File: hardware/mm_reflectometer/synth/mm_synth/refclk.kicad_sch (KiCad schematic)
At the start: 25 parts

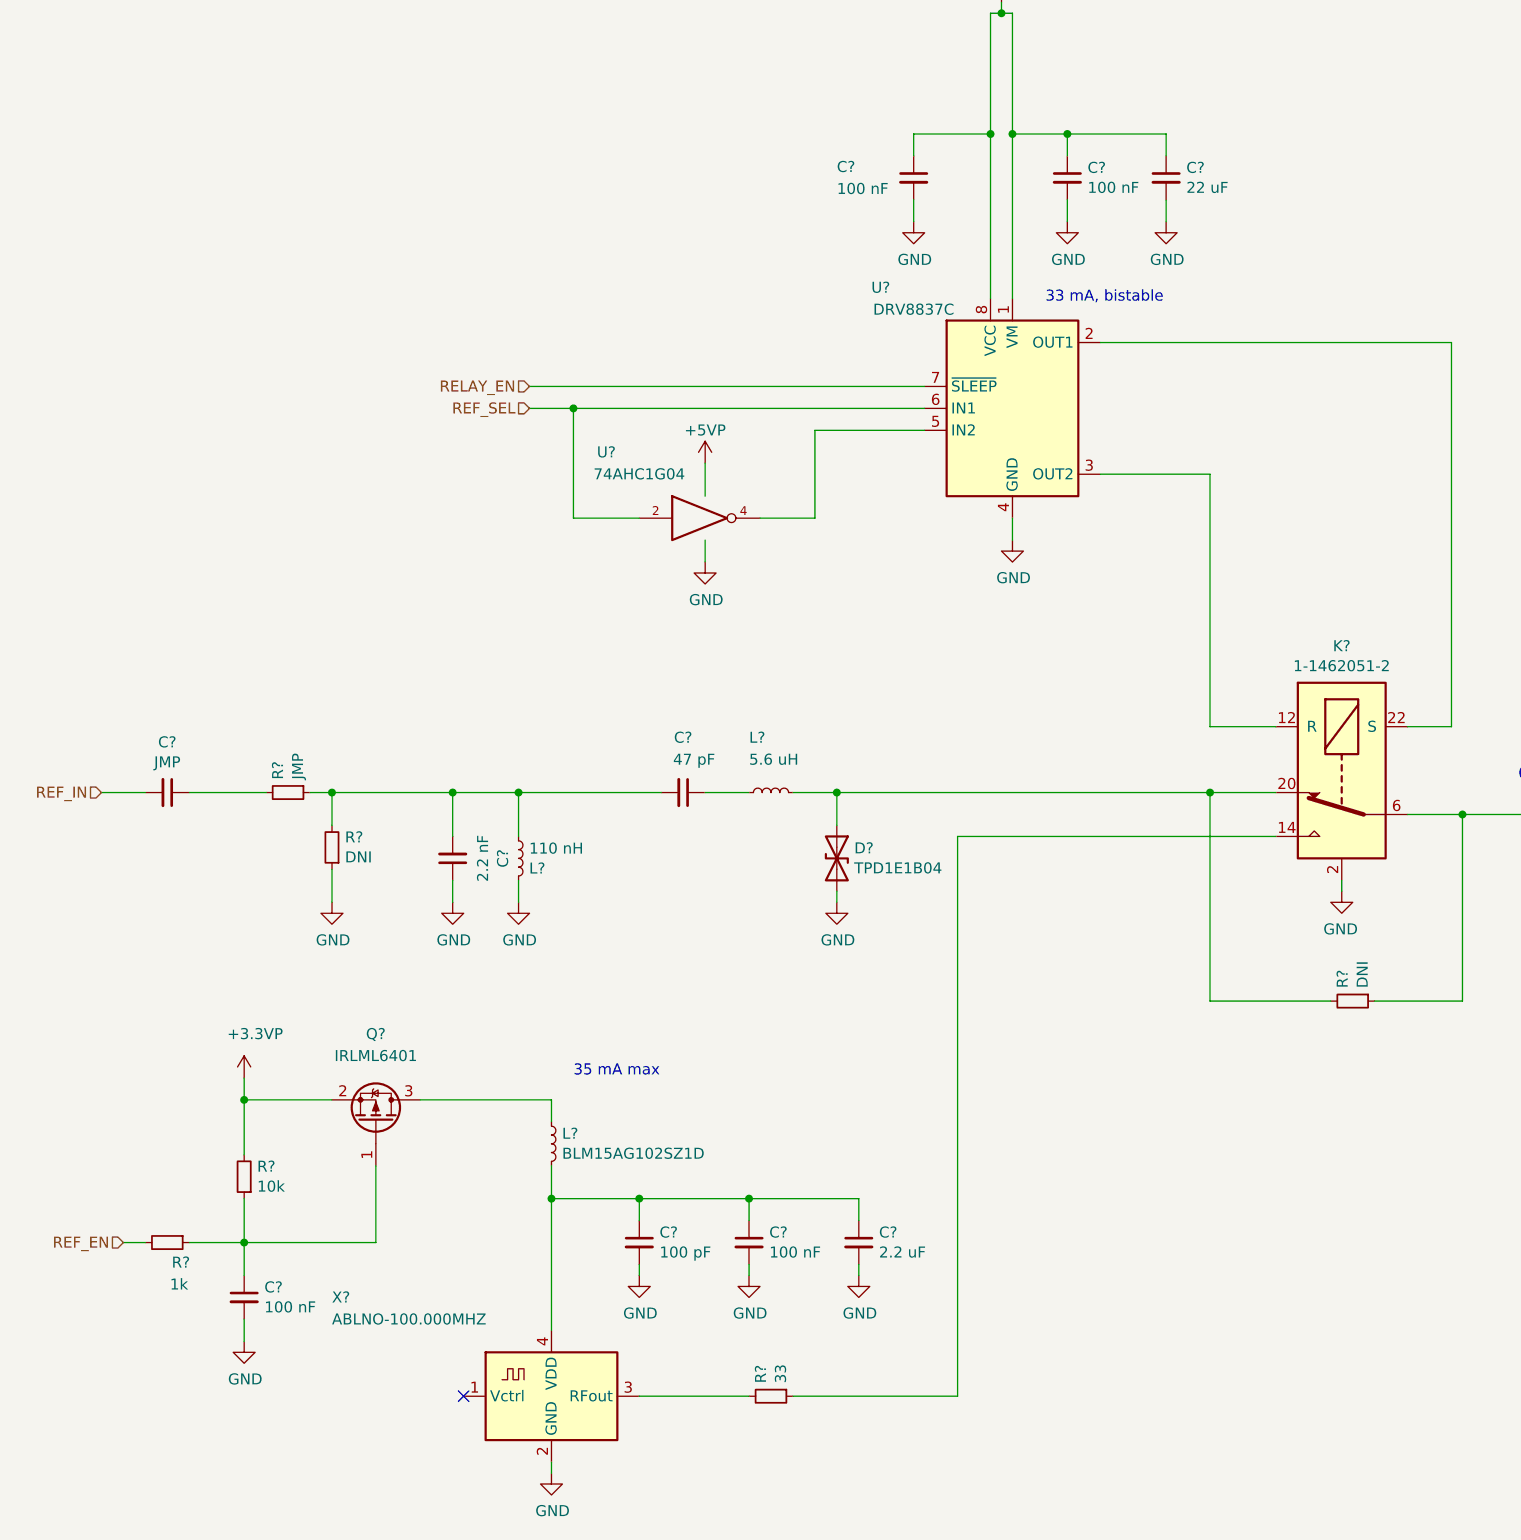
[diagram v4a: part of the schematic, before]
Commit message: work on mm synth schematic - control signals and footprint assignments
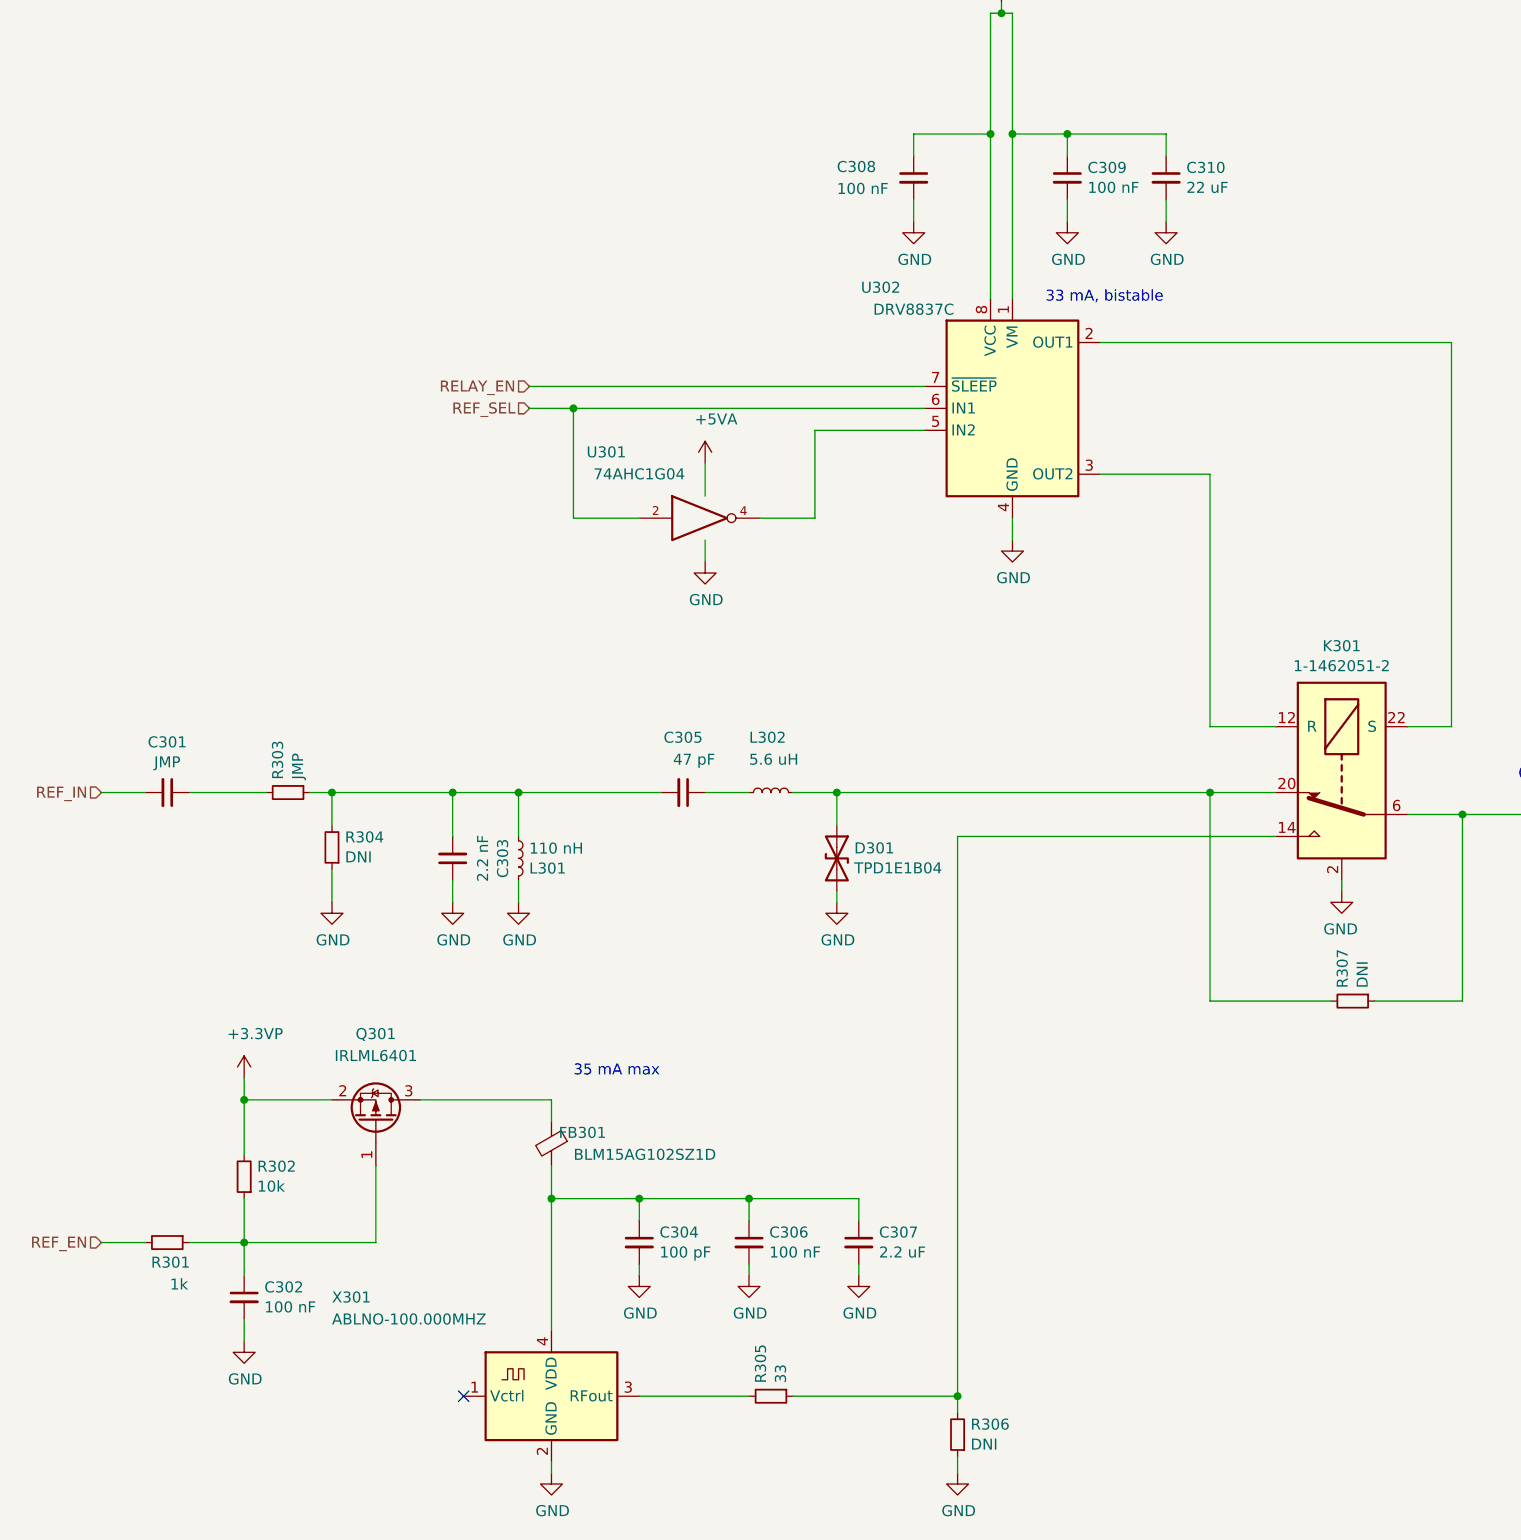
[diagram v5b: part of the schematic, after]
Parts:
- removed L?: BLM15AG102SZ1D, Inductor_SMD:L_0402_1005Metric, symbol Device:L_Small
- added FB301: BLM15AG102SZ1D, symbol Device:FerriteBead_Small
- added R306: DNI, Resistor_SMD:R_0402_1005Metric, symbol Device:R_Small
- gave numbers to parts that had none: 24
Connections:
- net +5VP is gone; now on net +5VA: U301.5 (VCC)
- net GND: now also R306.1
- net at Q301.3 (D): now also FB301.1
- net at C304.1, C306.1, C307.1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: now also FB301.2
- net at K301.14, R305.1: now also R306.2

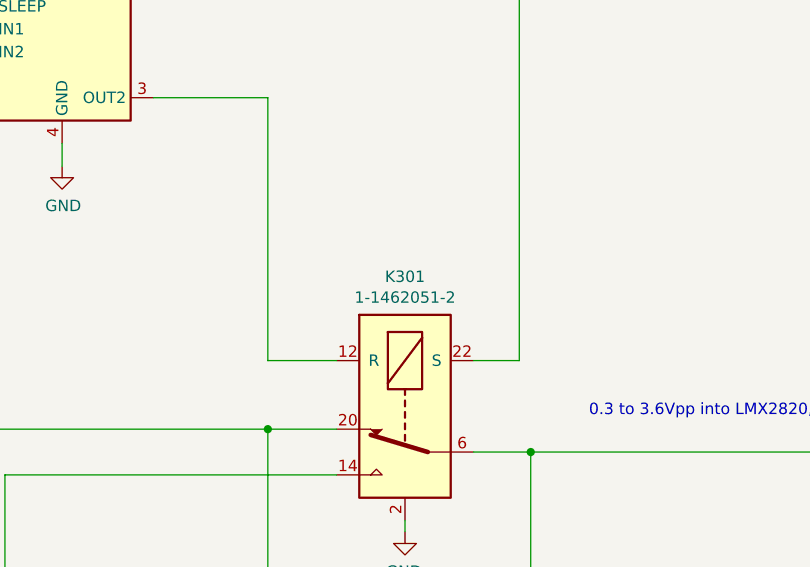
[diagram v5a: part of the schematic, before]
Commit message: added aux high speed io connector, fixed hierarchical buses
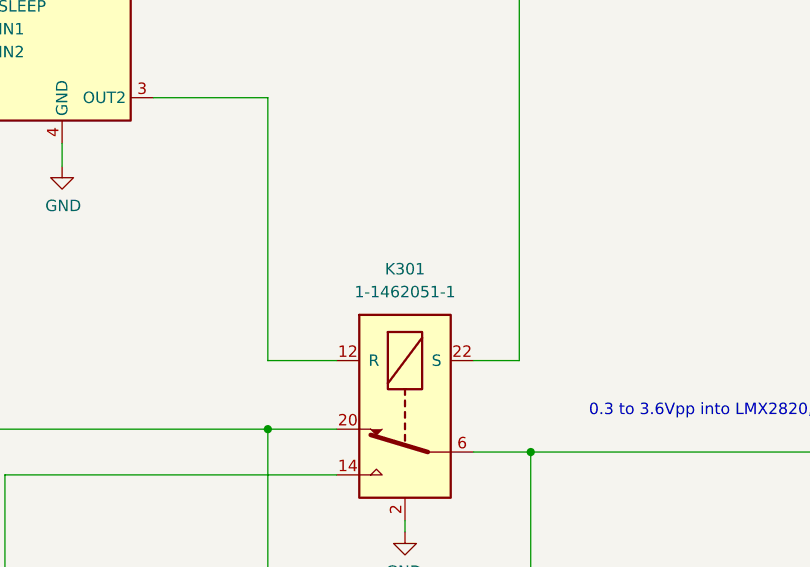
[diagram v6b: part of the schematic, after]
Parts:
- removed K301: 1-1462051-2, Relay_SMD:Relay_SPDT_AXICOM_HF3Series_50ohms_Pitch1.27mm, symbol vna_mm_ref-rescue:1-1462051-1-vna_mm
- added K301: 1-1462051-1, Relay_SMD:Relay_SPDT_AXICOM_HF3Series_50ohms_Pitch1.27mm, symbol vna_mm:1-1462051-1
- FB301: footprint (none) -> Inductor_SMD:L_0402_1005Metric
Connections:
- net GND: now also K301.10, K301.13, K301.15, K301.17, K301.19, K301.2, K301.21, K301.5, K301.7
- net OSC_OUT: now also K301.6
- net at U302.2 (OUT1): now also K301.11, K301.22 (S)
- net at U302.3 (OUT2): now also K301.1, K301.12 (R)
- net at R305.1, R306.2: now also K301.14
- net at D301.1 (A1), L302.1, R307.2: now also K301.20
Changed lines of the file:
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@@
       (effects (font (size 1.27 1.27)) (justify left))
     )
-    (property "Footprint" "" (id 2) (at 83.058 151.13 90)
+    (property "Footprint" "Inductor_SMD:L_0402_1005Metric" (id 2) (at 83.058 151.13 90)
       (effects (font (size 1.27 1.27)) hide)
     )
@@
     (pin "4")
   )
-  (symbol (lib_id "vna_mm_ref-rescue:1-1462051-1-vna_mm") (at 171.45 107.95 0) (mirror y) (unit 1)
-    (in_bom yes) (on_board yes)
-    (property "Reference" "K301" (id 0) (at 172.72 93.5482 0))
-    (property "Value" "1-1462051-2" (id 1) (at 172.72 95.8596 0))
+  (symbol (lib_id "vna_mm:1-1462051-1") (at 171.45 107.95 0) (mirror y) (unit 1)
+    (in_bom yes) (on_board yes) (fields_autoplaced)
+    (property "Reference" "K301" (id 0) (at 172.72 92.71 0))
+    (property "Value" "1-1462051-1" (id 1) (at 172.72 95.25 0))
     (property "Footprint" "Relay_SMD:Relay_SPDT_AXICOM_HF3Series_50ohms_Pitch1.27mm" (id 2) (at 182.88 93.98 0)
       (effects (font (size 1.27 1.27)) (justify left) hide)
@@
       (effects (font (size 1.27 1.27)) hide)
     )
-    (property "DIST_NAME" "Digi-Key" (id 4) (at 171.45 107.95 0)
-      (effects (font (size 1.27 1.27)) hide)
-    )
-    (property "DIST_PN" "41-1-1462051-1CT-ND" (id 5) (at 171.45 107.95 0)
-      (effects (font (size 1.27 1.27)) hide)
-    )
